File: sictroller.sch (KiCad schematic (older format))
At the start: 15 parts

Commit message: progress on V2 schematic
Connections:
- net Feedback/IFB_A renamed Feedback/~IFB_A
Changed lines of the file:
@@
 F4 "VFB_C" I L 4750 2100 60
 F5 "VFB_BUS" I L 4750 2200 60
-F6 "IFB_A" I L 4750 2350 60
-F7 "IFB_B" I L 4750 2450 60
-F8 "IFB_C" I L 4750 2550 60
-F9 "PWR_STG_TEMP" I L 4750 1650 60
-F10 "MOTOR_TEMP" I L 4750 1750 60
-F11 "IFB_BUS" I L 4750 2650 60
-F12 "PWM_AH" O R 7100 2350 60
-F13 "PWM_BH" O R 7100 2550 60
-F14 "PWM_CH" O R 7100 2750 60
-F15 "PWM_AL" O R 7100 2450 60
-F16 "PWM_BL" O R 7100 2650 60
-F17 "PWM_CL" O R 7100 2850 60
-F18 "~FLT_DESAT" I R 7100 1850 60
-F19 "~FLT_OTP" I R 7100 1950 60
-F20 "PWR_RDY" I R 7100 1650 60
-F21 "~PWR_RESET" O R 7100 2150 60
+F6 "IFB_B" I L 4750 2450 60
+F7 "IFB_C" I L 4750 2550 60
+F8 "PWM_AH" O R 7100 2350 60
+F9 "PWM_BH" O R 7100 2550 60
+F10 "PWM_CH" O R 7100 2750 60
+F11 "PWM_AL" O R 7100 2450 60
+F12 "PWM_BL" O R 7100 2650 60
+F13 "PWM_CL" O R 7100 2850 60
+F14 "~FLT_DESAT" I R 7100 1850 60
+F15 "~FLT_OTP" I R 7100 1950 60
+F16 "PWR_RDY" I R 7100 1650 60
+F17 "~PWR_RESET" O R 7100 2150 60
+F18 "~IFB_A" I L 4750 2350 60
+F19 "TEMP_PWM" I L 4750 1650 60
+F20 "TEMP_EN" O L 4750 1750 60
 $EndSheet
 $Sheet
@@
 F3 "VFB_B" O R 3850 2000 60
 F4 "VFB_C" O R 3850 2100 60
-F5 "IFB_A" O R 3850 2350 60
-F6 "IFB_B" O R 3850 2450 60
-F7 "IFB_C" O R 3850 2550 60
-F8 "VFB_BUS" O R 3850 2200 60
-F9 "PWR_TEMP" O R 3850 1650 60
-F10 "MOTOR_TEMP" O R 3850 1750 60
-F11 "IFB_BUS" O R 3850 2650 60
+F5 "IFB_B" O R 3850 2450 60
+F6 "IFB_C" O R 3850 2550 60
+F7 "VFB_BUS" O R 3850 2200 60
+F8 "~IFB_A" O R 3850 2350 60
+F9 "TEMP_PWM" O R 3850 1650 60
+F10 "TEMP_EN" I R 3850 1750 60
 $EndSheet
 $Sheet
-S 7950 1500 1150 1500
+S 7950 1500 1150 1850
 U 57A1662D
 F0 "Power stage" 60
 F1 "powerstage-CCS050M12CM2.sch" 60
-F2 "PWR_RDY" O L 7950 1650 60
-F3 "~PWR_RESET" I L 7950 2150 60
-F4 "PWM_AH" I L 7950 2350 60
-F5 "PWM_AL" I L 7950 2450 60
-F6 "PWM_BH" I L 7950 2550 60
-F7 "PWM_BL" I L 7950 2650 60
-F8 "PWM_CH" I L 7950 2750 60
-F9 "PWM_CL" I L 7950 2850 60
-F10 "~FLT_DESAT" O L 7950 1850 60
-F11 "~FLT_OTP" O L 7950 1950 60
+F2 "~PWR_RESET" I L 7950 2150 60
+F3 "PWM_AH" I L 7950 2350 60
+F4 "PWM_AL" I L 7950 2450 60
+F5 "PWM_BH" I L 7950 2550 60
+F6 "PWM_BL" I L 7950 2650 60
+F7 "PWM_CH" I L 7950 2750 60
+F8 "PWM_CL" I L 7950 2850 60
+F9 "~FLT_DESAT" O L 7950 1850 60
+F10 "~GDRV_RDY" O L 7950 1650 60
 $EndSheet
 Wire Wire Line
@@
 	3850 2550 4750 2550
 Wire Wire Line
-	4750 2650 3850 2650
-Wire Wire Line
 	7950 2150 7100 2150
 Wire Wire Line
-	7100 1950 7950 1950
-Wire Wire Line
 	7950 1850 7100 1850

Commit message: further V2 progress
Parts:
- removed W21, W22, W23: TEST_1P, Measurement_Points:Measurement_Point_Round-SMD-Pad_Small, symbol TEST_1P
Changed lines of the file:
@@
-$EndComp
-$Comp
-L TEST_1P W22
-U 1 1 57A8946B
-P 7700 2550
-F 0 "W22" H 7750 2700 50  0000 L CNN
-F 1 "TEST_1P" H 7758 2579 50  0001 L CNN
-F 2 "Measurement_Points:Measurement_Point_Round-SMD-Pad_Small" H 7900 2550 50  0001 C CNN
-F 3 "" H 7900 2550 50  0000 C CNN
-	1    7700 2550
-	1    0    0    -1
 $EndComp
 $Comp
@@
 	-1   0    0    1
 $EndComp
-$Comp
-L TEST_1P W21
-U 1 1 57A8A1F8
-P 7500 2750
-F 0 "W21" H 7550 2900 50  0000 L CNN
-F 1 "TEST_1P" H 7558 2779 50  0001 L CNN
-F 2 "Measurement_Points:Measurement_Point_Round-SMD-Pad_Small" H 7700 2750 50  0001 C CNN
-F 3 "" H 7700 2750 50  0000 C CNN
-	1    7500 2750
-	-1   0    0    1
-$EndComp
-$Comp
-L TEST_1P W23
-U 1 1 57A8A46D
-P 7700 2850
-F 0 "W23" H 7750 3000 50  0000 L CNN
-F 1 "TEST_1P" H 7758 2879 50  0001 L CNN
-F 2 "Measurement_Points:Measurement_Point_Round-SMD-Pad_Small" H 7900 2850 50  0001 C CNN
-F 3 "" H 7900 2850 50  0000 C CNN
-	1    7700 2850
-	-1   0    0    1
-$EndComp
-Connection ~ 7700 2850
-Connection ~ 7500 2750
 Connection ~ 7300 2650
-Connection ~ 7700 2550
 Connection ~ 7500 2450
 Connection ~ 7300 2350

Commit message: V2 schem complete, footprints not assigned
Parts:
- renumbered W8 to W1, W4 to W10, W5 to W11, W6 to W12, W10 to W2, W13 to W3, W16 to W4, W9 to W5, W18 to W6, W20 to W7, W19 to W8, W3 to W9
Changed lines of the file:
@@
 LIBS:TMDSCNCD28069
 LIBS:74LVC8T245
+LIBS:viper0p-etc
 LIBS:sictroller-cache
 EELAYER 25 0
@@
 F13 "PWM_CL" O R 7100 2850 60
 F14 "~FLT_DESAT" I R 7100 1850 60
-F15 "~FLT_OTP" I R 7100 1950 60
-F16 "PWR_RDY" I R 7100 1650 60
-F17 "~PWR_RESET" O R 7100 2150 60
-F18 "~IFB_A" I L 4750 2350 60
-F19 "TEMP_PWM" I L 4750 1650 60
-F20 "TEMP_EN" O L 4750 1750 60
+F15 "PWR_RDY" I R 7100 1650 60
+F16 "~PWR_RESET" O R 7100 2150 60
+F17 "~IFB_A" I L 4750 2350 60
+F18 "TEMP_PWM" I L 4750 1650 60
+F19 "TEMP_EN" O L 4750 1750 60
 $EndSheet
 $Sheet
@@
 	7100 1650 7950 1650
 $Comp
-L TEST_1P W3
+L TEST_1P W9
 U 1 1 57A83AEA
 P 800 7550
-F 0 "W3" H 858 7670 50  0000 L CNN
+F 0 "W9" H 858 7670 50  0000 L CNN
 F 1 "TEST_1P" H 858 7579 50  0000 L CNN
 F 2 "Measurement_Points:Measurement_Point_Round-TH_Small" H 1000 7550 50  0001 C CNN
@@
 $EndComp
 $Comp
-L TEST_1P W4
+L TEST_1P W10
 U 1 1 57A83CBB
 P 1200 7550
-F 0 "W4" H 1258 7670 50  0000 L CNN
+F 0 "W10" H 1258 7670 50  0000 L CNN
 F 1 "TEST_1P" H 1258 7579 50  0000 L CNN
 F 2 "Measurement_Points:Measurement_Point_Round-TH_Small" H 1400 7550 50  0001 C CNN
@@
 $EndComp
 $Comp
-L TEST_1P W5
+L TEST_1P W11
 U 1 1 57A84AD6
 P 1600 7550
-F 0 "W5" H 1658 7670 50  0000 L CNN
+F 0 "W11" H 1658 7670 50  0000 L CNN
 F 1 "TEST_1P" H 1658 7579 50  0000 L CNN
 F 2 "Measurement_Points:Measurement_Point_Round-TH_Small" H 1800 7550 50  0001 C CNN
@@
 $EndComp
 $Comp
-L TEST_1P W6
+L TEST_1P W12
 U 1 1 57A84ADC
 P 2000 7550
-F 0 "W6" H 2058 7670 50  0000 L CNN
+F 0 "W12" H 2058 7670 50  0000 L CNN
 F 1 "TEST_1P" H 2058 7579 50  0000 L CNN
 F 2 "Measurement_Points:Measurement_Point_Round-TH_Small" H 2200 7550 50  0001 C CNN
@@
 $EndComp
 $Comp
-L TEST_1P W18
+L TEST_1P W6
 U 1 1 57A85972
 P 7300 2350
-F 0 "W18" H 7350 2450 50  0000 L CNN
+F 0 "W6" H 7350 2450 50  0000 L CNN
 F 1 "TEST_1P" H 7358 2379 50  0001 L CNN
 F 2 "Measurement_Points:Measurement_Point_Round-TH_Small" H 7500 2350 50  0001 C CNN
@@
 $EndComp
 $Comp
-L TEST_1P W20
+L TEST_1P W7
 U 1 1 57A89327
 P 7500 2450
-F 0 "W20" H 7550 2600 50  0000 L CNN
+F 0 "W7" H 7550 2600 50  0000 L CNN
 F 1 "TEST_1P" H 7558 2479 50  0001 L CNN
 F 2 "Measurement_Points:Measurement_Point_Round-TH_Small" H 7700 2450 50  0001 C CNN
@@
 $EndComp
 $Comp
-L TEST_1P W19
+L TEST_1P W8
 U 1 1 57A89F70
 P 7300 2650
-F 0 "W19" H 7350 2800 50  0000 L CNN
+F 0 "W8" H 7350 2800 50  0000 L CNN
 F 1 "TEST_1P" H 7358 2679 50  0001 L CNN
 F 2 "Measurement_Points:Measurement_Point_Round-SMD-Pad_Small" H 7500 2650 50  0001 C CNN
@@
 Connection ~ 7300 2350
 $Comp
-L TEST_1P W8
+L TEST_1P W1
 U 1 1 57A8E259
 P 4100 1900
-F 0 "W8" H 4150 2050 50  0000 L CNN
+F 0 "W1" H 4150 2050 50  0000 L CNN
 F 1 "TEST_1P" H 4158 1929 50  0001 L CNN
 F 2 "Measurement_Points:Measurement_Point_Round-TH_Small" H 4300 1900 50  0001 C CNN
@@
 $EndComp
 $Comp
-L TEST_1P W10
+L TEST_1P W2
 U 1 1 57A8E4FF
 P 4250 2000
-F 0 "W10" H 4300 2150 50  0000 L CNN
+F 0 "W2" H 4300 2150 50  0000 L CNN
 F 1 "TEST_1P" H 4308 2029 50  0001 L CNN
 F 2 "Measurement_Points:Measurement_Point_Round-SMD-Pad_Small" H 4450 2000 50  0001 C CNN
@@
 $EndComp
 $Comp
-L TEST_1P W13
+L TEST_1P W3
 U 1 1 57A8E7A8
 P 4400 2100
-F 0 "W13" H 4450 2250 50  0000 L CNN
+F 0 "W3" H 4450 2250 50  0000 L CNN
 F 1 "TEST_1P" H 4458 2129 50  0001 L CNN
 F 2 "Measurement_Points:Measurement_Point_Round-SMD-Pad_Small" H 4600 2100 50  0001 C CNN
@@
 $EndComp
 $Comp
-L TEST_1P W16
+L TEST_1P W4
 U 1 1 57A8EA5A
 P 4550 2200
-F 0 "W16" H 4600 2350 50  0000 L CNN
+F 0 "W4" H 4600 2350 50  0000 L CNN
 F 1 "TEST_1P" H 4608 2229 50  0001 L CNN
 F 2 "Measurement_Points:Measurement_Point_Round-SMD-Pad_Small" H 4750 2200 50  0001 C CNN
@@
 $EndComp
 $Comp
-L TEST_1P W9
+L TEST_1P W5
 U 1 1 57A8EFB5
 P 4100 2350
-F 0 "W9" H 4150 2500 50  0000 L CNN
+F 0 "W5" H 4150 2500 50  0000 L CNN
 F 1 "TEST_1P" H 4158 2379 50  0001 L CNN
 F 2 "Measurement_Points:Measurement_Point_Round-TH_Small" H 4300 2350 50  0001 C CNN

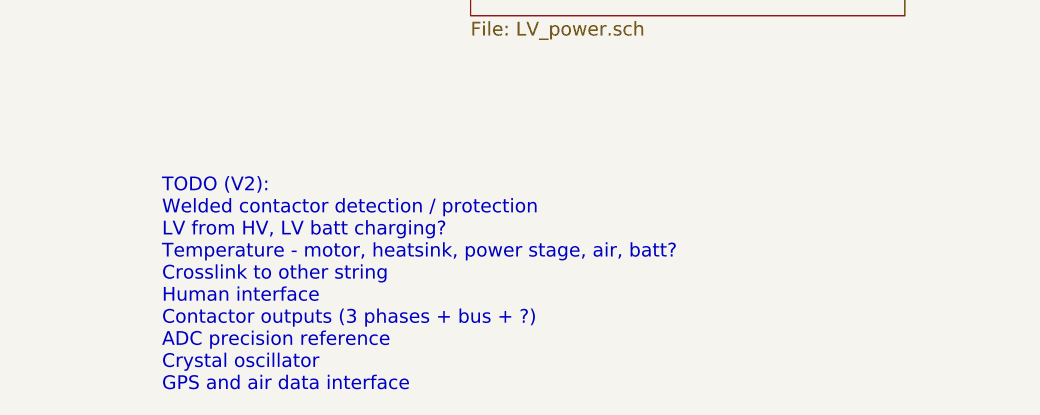
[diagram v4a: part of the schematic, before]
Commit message: Footprints assigned for all except halfbridge-driver
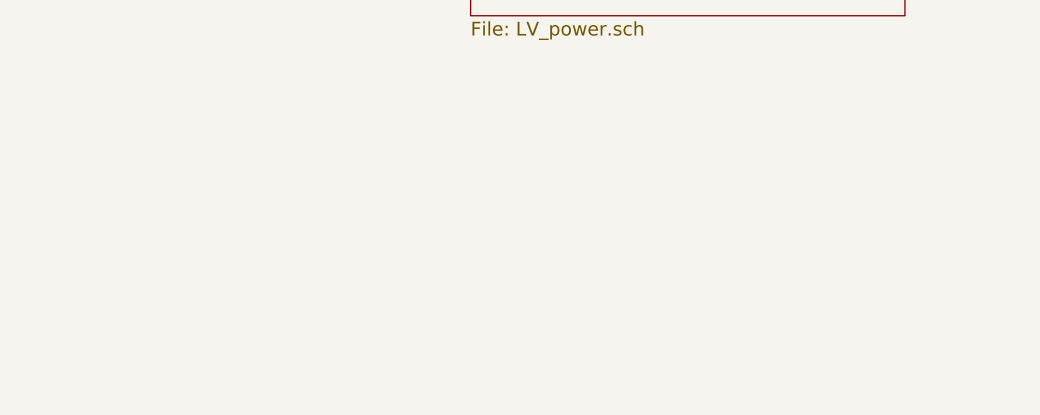
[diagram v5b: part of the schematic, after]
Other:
- note removed: "TODO (V2):\nWelded contactor detection / protection\nLV from HV, LV batt charging?\nTemperature - motor, heatsink, power stage, air, batt?\nCrosslink to other string\nHuman interface\nContactor outputs (3 phases + bus + ?)\nADC precision reference\nCrystal oscillator\nGPS and air data interface"
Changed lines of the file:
@@
 Comment4 ""
 $EndDescr
-Text Notes 3600 7900 0    60   ~ 0
-TODO (V2):\nWelded contactor detection / protection\nLV from HV, LV batt charging?\nTemperature - motor, heatsink, power stage, air, batt?\nCrosslink to other string\nHuman interface\nContactor outputs (3 phases + bus + ?)\nADC precision reference\nCrystal oscillator\nGPS and air data interface
 $Sheet
 S 4750 1500 2350 1850

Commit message: some logic placement progress
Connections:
- net GNDD: no longer W11.1, W12.1
- new net GNDA: W11.1, W12.1
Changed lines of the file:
@@
-$EndComp
-$Comp
-L GNDD #PWR03
-U 1 1 57A84AE2
-P 1600 7550
-F 0 "#PWR03" H 1600 7300 50  0001 C CNN
-F 1 "GNDD" H 1605 7377 50  0000 C CNN
-F 2 "" H 1600 7550 50  0000 C CNN
-F 3 "" H 1600 7550 50  0000 C CNN
-	1    1600 7550
-	1    0    0    -1
-$EndComp
-$Comp
-L GNDD #PWR04
-U 1 1 57A84AE8
-P 2000 7550
-F 0 "#PWR04" H 2000 7300 50  0001 C CNN
-F 1 "GNDD" H 2005 7377 50  0000 C CNN
-F 2 "" H 2000 7550 50  0000 C CNN
-F 3 "" H 2000 7550 50  0000 C CNN
-	1    2000 7550
-	1    0    0    -1
 $EndComp
 $Comp
@@
 Connection ~ 4550 2200
 Connection ~ 4100 2350
+$Comp
+L GNDA #PWR03
+U 1 1 5806E9BD
+P 2000 7550
+F 0 "#PWR03" H 2000 7300 50  0001 C CNN
+F 1 "GNDA" H 2000 7400 50  0000 C CNN
+F 2 "" H 2000 7550 50  0000 C CNN
+F 3 "" H 2000 7550 50  0000 C CNN
+	1    2000 7550
+	1    0    0    -1
+$EndComp
+$Comp
+L GNDA #PWR04
+U 1 1 5806ED9E
+P 1600 7550
+F 0 "#PWR04" H 1600 7300 50  0001 C CNN
+F 1 "GNDA" H 1600 7400 50  0000 C CNN
+F 2 "" H 1600 7550 50  0000 C CNN
+F 3 "" H 1600 7550 50  0000 C CNN
+	1    1600 7550
+	1    0    0    -1
+$EndComp
 $EndSCHEMATC
